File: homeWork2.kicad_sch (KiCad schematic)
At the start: 47 parts, among them J1 Barrel_Jack_Switch_SMT, J2 0.100_2Pin, J3 0.100_2Pin, U1 LM7805_TO220

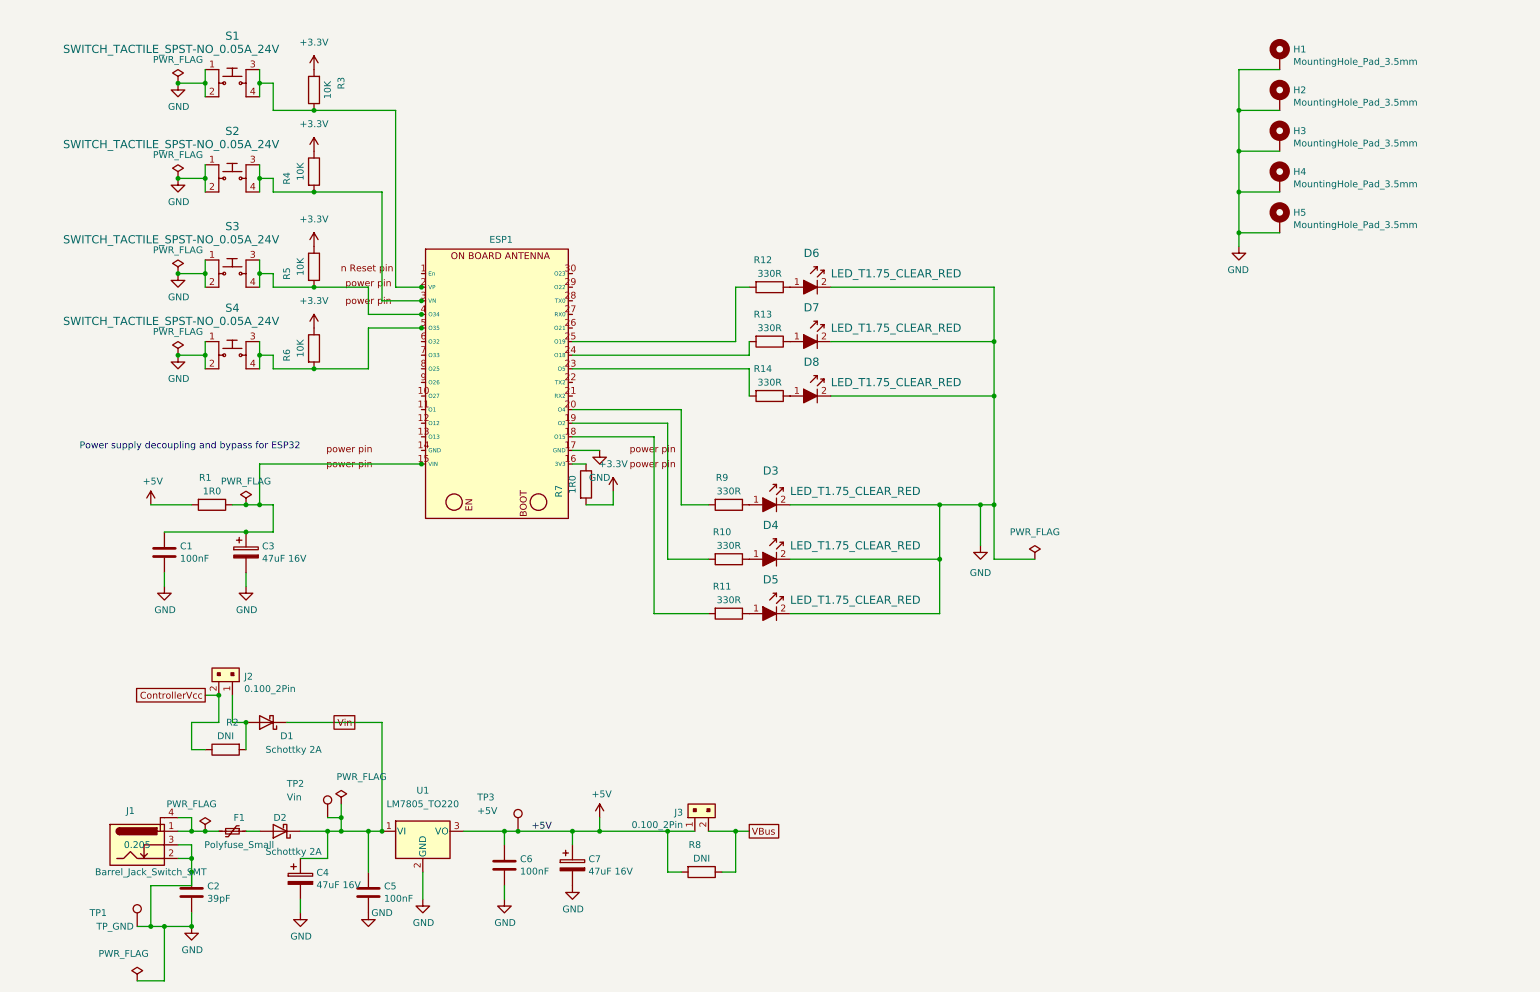
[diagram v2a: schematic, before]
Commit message: this is to clean the deleted backup files and to update the modified pcb file where I attached the copper fill to ground and added text to the silkscreen and to update the sch files where I added the date and the serial number space in the origin main branch.
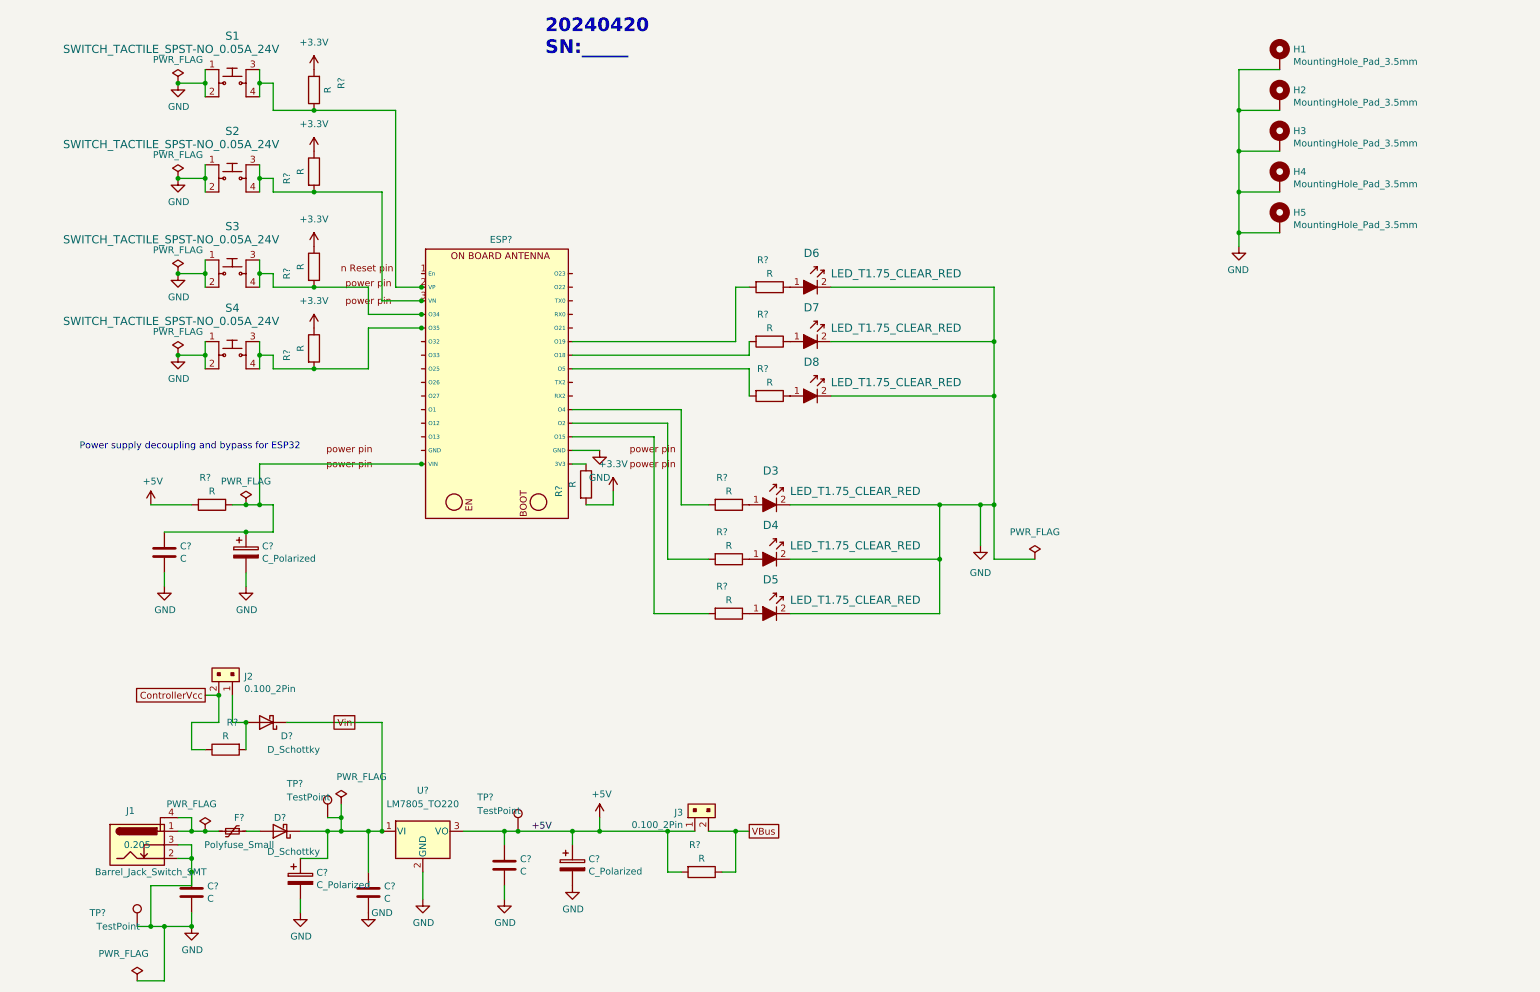
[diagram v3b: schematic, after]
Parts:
- C?: renamed from C6; value 100nF -> C
- C?: renamed from C5; value 100nF -> C
- C?: renamed from C7; value 47uF 16V -> C_Polarized
- C?: renamed from C2; value 39pF -> C
- C?: renamed from C4; value 47uF 16V -> C_Polarized
- C?: renamed from C3; value 47uF 16V -> C_Polarized
- C?: renamed from C1; value 100nF -> C
- D?: renamed from D2; value Schottky 2A -> D_Schottky
- D?: renamed from D1; value Schottky 2A -> D_Schottky
- R?: renamed from R10; value 330R -> R
- R?: renamed from R6; value 10K -> R
- R?: renamed from R8; value DNI -> R
- R?: renamed from R3; value 10K -> R
- R?: renamed from R5; value 10K -> R
- R?: renamed from R13; value 330R -> R
- R?: renamed from R9; value 330R -> R
- R?: renamed from R12; value 330R -> R
- R?: renamed from R11; value 330R -> R
- R?: renamed from R7; value 1R0 -> R
- R?: renamed from R2; value DNI -> R
- R?: renamed from R4; value 10K -> R
- R?: renamed from R1; value 1R0 -> R
- R?: renamed from R14; value 330R -> R
- TP?: renamed from TP1; value TP_GND -> TestPoint
- TP?: renamed from TP2; value Vin -> TestPoint
- TP?: renamed from TP3; value +5V -> TestPoint
- renumbered ESP1 to ESP?, F1 to F?, U1 to U?
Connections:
- net GND: now also ESP?. (VIN); no longer ESP?.17 (GND)
- net at R?.2: now also ESP?. (VIN); no longer ESP?.19 (O2)
- net at C?.1, C?.1, R?.1: now also ESP?. (VIN); no longer ESP?.15 (VIN)
- net at R?.1: now also ESP?. (VIN); no longer ESP?.16 (3V3)
- net at R?.2: now also ESP?. (VIN); no longer ESP?.18 (O15)
- net at R?.2: now also ESP?. (VIN); no longer ESP?.20 (O4)
- net at R?.2: now also ESP?. (VIN); no longer ESP?.23 (O5)
- net at R?.2: now also ESP?. (VIN); no longer ESP?.24 (O18)
- net at R?.2: now also ESP?. (VIN); no longer ESP?.25 (O19)
- net at R?.2, S3.3, S3.4: now also ESP?. (VIN); no longer ESP?.4 (O34)
- net at R?.2, S4.3, S4.4: now also ESP?. (VIN); no longer ESP?.5 (O35)
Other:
- note added: "20240420 SN:_____"

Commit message: I updated the ESP32 footprint and symbol, renamed the pins of the ESP32 in a clockwise direction. I rerouted the copper, and ran a DRC test with zero errors and refined the edge cut of the board to make it smaller and neater.
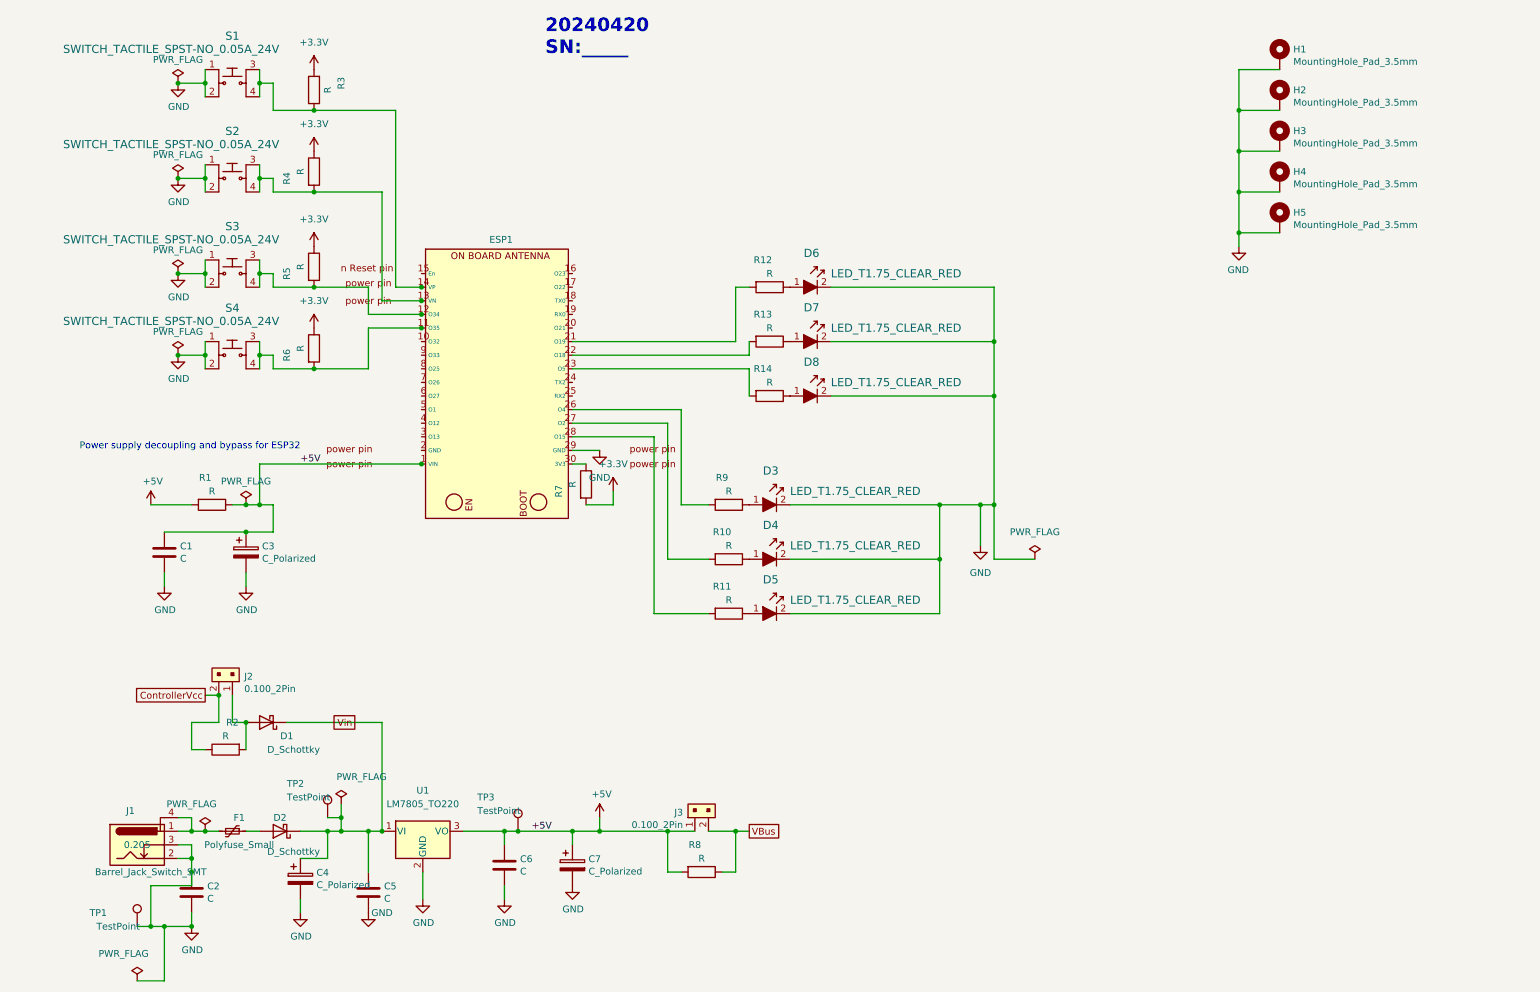
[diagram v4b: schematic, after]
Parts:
- gave numbers to parts that had none: 29
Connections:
- net +5V: now also C1.1, C3.1, ESP1.1 (VIN), R1.1
- net GND: now also ESP1.29 (GND); no longer ESP1. (VIN)
- net at R10.2: now also ESP1.27 (O2); no longer ESP1. (VIN)
- net at R6.2, S4.3, S4.4: now also ESP1.11 (O35); no longer ESP1. (VIN)
- net at R5.2, S3.3, S3.4: now also ESP1.12 (O34); no longer ESP1. (VIN)
- net at R13.2: now also ESP1.22 (O18); no longer ESP1. (VIN)
- net at R9.2: now also ESP1.26 (O4); no longer ESP1. (VIN)
- net at R12.2: now also ESP1.21 (O19); no longer ESP1. (VIN)
- net at R11.2: now also ESP1.28 (O15); no longer ESP1. (VIN)
- net at R7.1: now also ESP1.30 (3V3); no longer ESP1. (VIN)
- net at R14.2: now also ESP1.23 (O5); no longer ESP1. (VIN)
- net at R3.1, S1.3, S1.4: now also ESP1.14 (VP); no longer ESP1.2 (VP)
- net at R4.2, S2.3, S2.4: now also ESP1.13 (VN); no longer ESP1.3 (VN)

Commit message: Four Net Classes are added, default, ground, and two classes for power, one for 5 volts and another for 3.3 volts.The width of the traces used allows 40 degrees Celius temperature rise of the component.
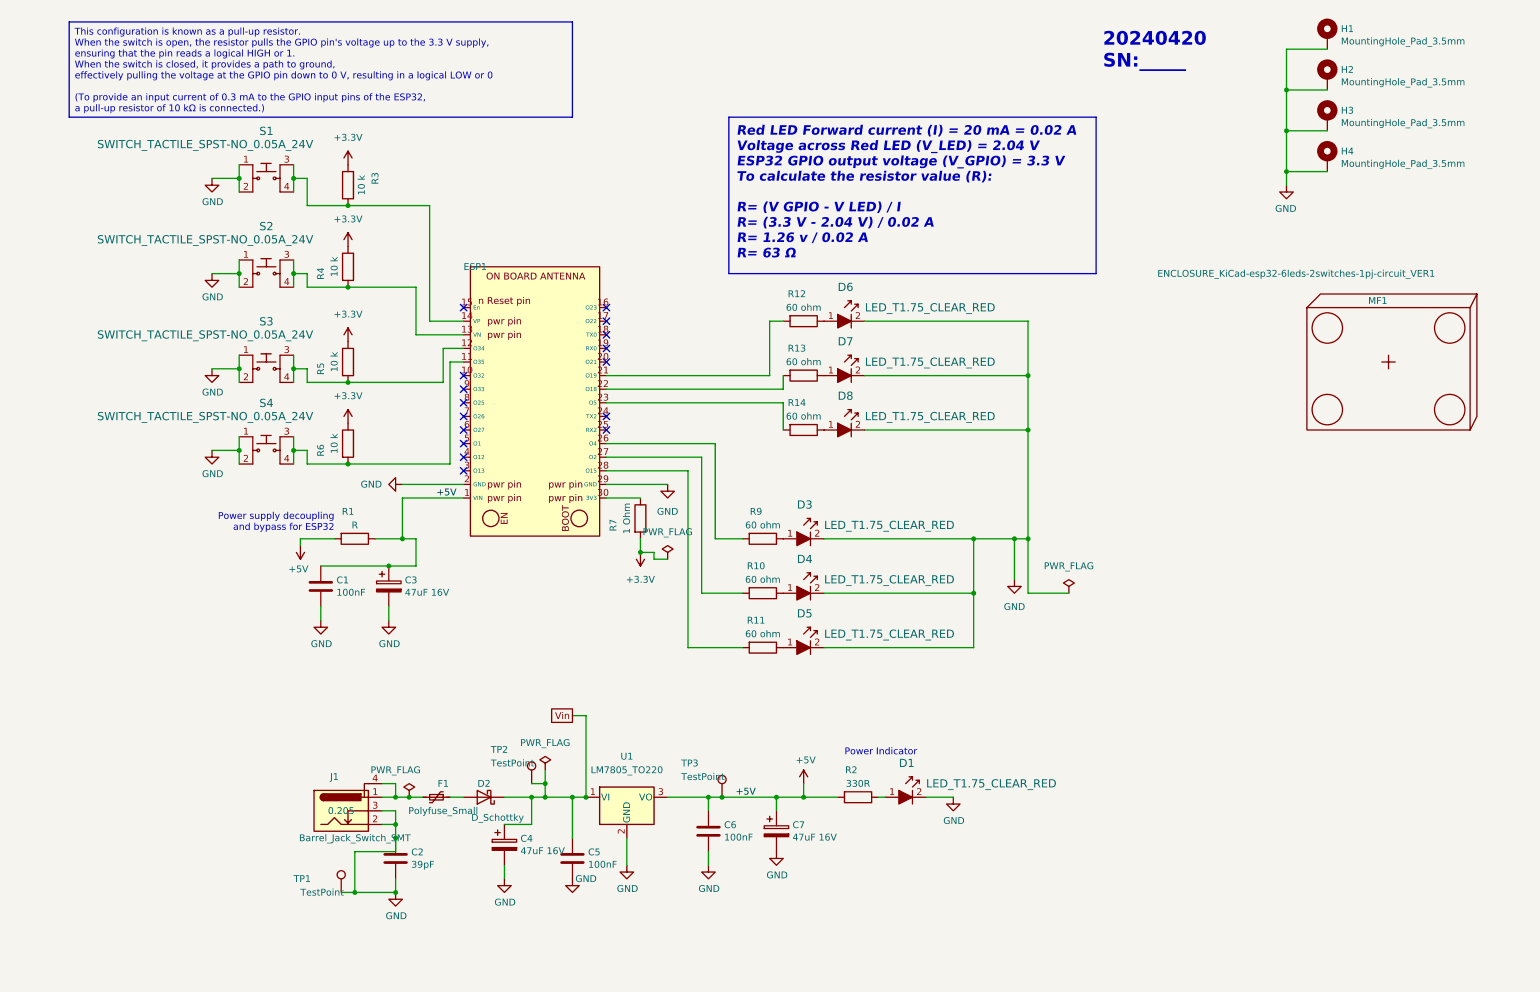
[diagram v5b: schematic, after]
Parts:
- removed D1: D_Schottky, Diode_SMD:D_SMB, symbol Device:D_Schottky
- removed H5: MountingHole_Pad_3.5mm, PubInv_KiCad_PCB:MountingHole_3.5mm_Pad_Via, symbol GPAD_SCH_LIB:MountingHole_Pad_3.5mm
- removed J2, J3: 0.100_2Pin, Connector_PinHeader_2.54mm:PinHeader_1x02_P2.54mm_Vertical, symbol GPAD_SCH_LIB:22-23-2021
- removed R8: R, Resistor_SMD:R_0603_1608Metric_Pad0.98x0.95mm_HandSolder, symbol Device:R
- added D1: LED_T1.75_CLEAR_RED, GeneralPurposeAlarmDevicePCB:LED_5mm_Radial, symbol GPAD_SCH_LIB:LED_T1.75_CLEAR_WHITE
- added MF1: ENCLOSURE_KiCad-esp32-6leds-2switches-1pj-circuit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, symbol GPAD_SCH_LIB:ENCLOSURE_GPAD_VER1
- C1, C5, C6: value C -> 100nF
- C2: value C -> 39pF
- C3, C4, C7: value C_Polarized -> 47uF 16V
- R10, R11, R12, R13, R14, R9: value R -> 60 ohm
- R2: value R -> 330R; Distributor 1 DNI -> JLCPCB; Distributor 1 PN DNI -> C269711; MPN DNI -> RMC06033301%N
- R3, R4, R5, R6: value R -> 10 k
- R7: value R -> 1 Ohm
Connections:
- net +5V: now also R2.2
- net GND: now also ESP1.2 (GND), D1.2
- net ControllerVcc: no longer names the net of R2.1
- net ControllerVcc: now also D1.1
- no-connect marks 0 -> 16
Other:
- note added: "Power Indicator"
- moved on the sheet: C1, C2, C3, C4, C5, C6, C7, D2, D3, D4, D5, D6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

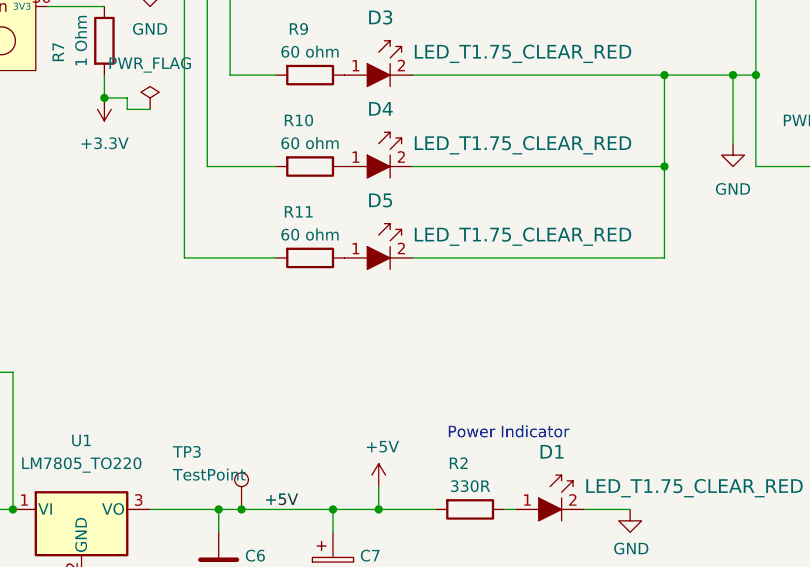
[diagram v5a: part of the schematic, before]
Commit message: Added text box capturing the calculations for setting the currect in LED.
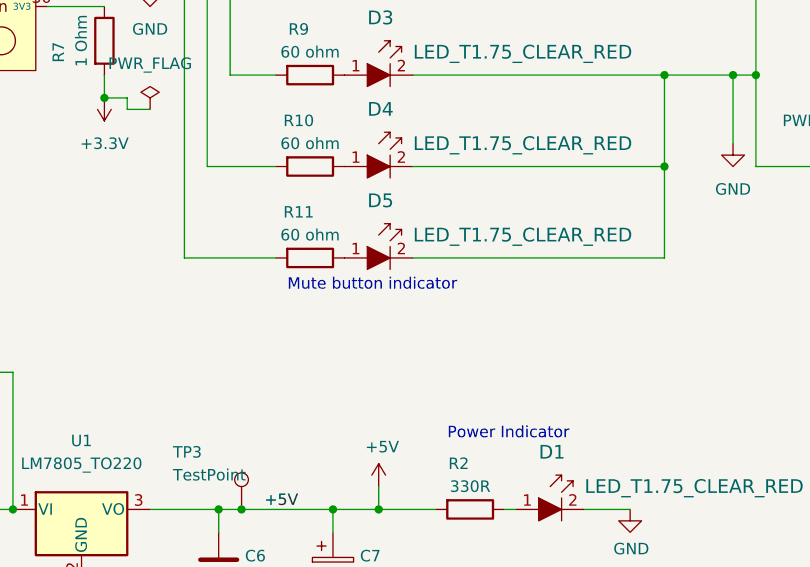
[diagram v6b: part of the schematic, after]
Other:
- note added: "Mute button indicator"
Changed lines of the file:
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@@
+    (stroke (width 0) (type default))
+  )
+  (wire (pts (xy 82.55 102.87) (xy 93.98 102.87))
     (stroke (width 0) (type default))
   )
@@
     (stroke (width 0) (type default))
   )
+  (wire (pts (xy 87.63 69.85) (xy 93.98 69.85))
+    (stroke (width 0) (type default))
+  )
   (wire (pts (xy 81.28 173.99) (xy 81.28 176.53))
     (stroke (width 0) (type default))
@@
     (stroke (width 0) (type default))
   )
-  (wire (pts (xy 87.63 69.85) (xy 93.98 69.85))
-    (stroke (width 0) (type default))
-  )
   (wire (pts (xy 46.99 93.98) (xy 52.07 93.98))
     (stroke (width 0) (type default))
@@
   )
   (wire (pts (xy 247.65 26.67) (xy 247.65 34.29))
-    (stroke (width 0) (type default))
-  )
-  (wire (pts (xy 82.55 102.87) (xy 93.98 102.87))
     (stroke (width 0) (type default))
   )
@@
     (effects (font (size 1.27 1.27)) (justify left top))
   )
+  (text "Mute button indicator" (at 147.32 134.62 0)
+    (effects (font (size 1.27 1.27)) (justify left bottom))
+  )
   (text "20240420\nSN:_____\n" (at 213.36 22.86 0)
